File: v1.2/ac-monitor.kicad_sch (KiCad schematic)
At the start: 5 parts, among them U5 MID400

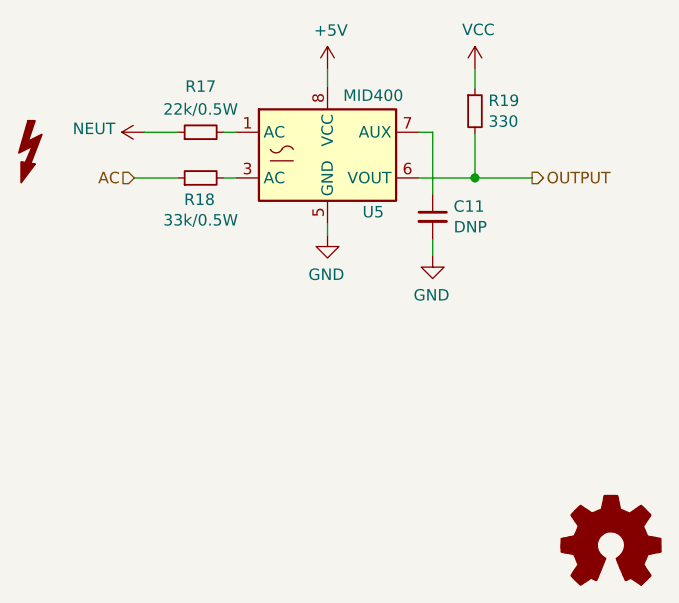
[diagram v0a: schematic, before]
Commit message: place debounce caps for mid400
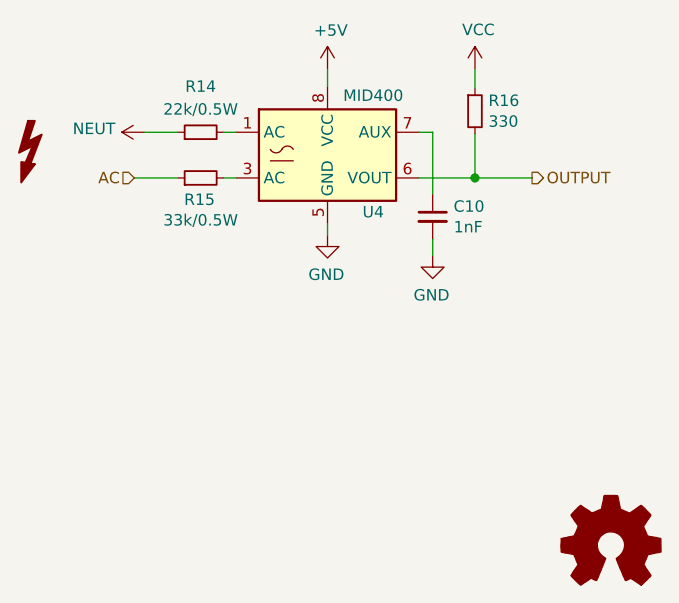
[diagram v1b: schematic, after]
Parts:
- C10: renamed from C11; value DNP -> 1nF
- renumbered R17 to R14, R18 to R15, R19 to R16, U5 to U4
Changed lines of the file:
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@@
   (symbol (lib_id "power:NEUT") (at 83.82 66.04 90)
     (in_bom yes) (on_board yes)
-    (property "Reference" "#PWR040" (id 0) (at 87.63 66.04 0)
+    (property "Reference" "#PWR035" (id 0) (at 87.63 66.04 0)
       (effects (font (size 1.27 1.27)) hide)
     )
@@
   (symbol (lib_id "power:+5V") (at 104.14 59.055 0)
     (in_bom yes) (on_board yes)
-    (property "Reference" "#PWR041" (id 0) (at 104.14 62.865 0)
+    (property "Reference" "#PWR036" (id 0) (at 104.14 62.865 0)
       (effects (font (size 1.27 1.27)) hide)
     )
@@
   (symbol (lib_id "power:VCC") (at 120.523 59.055 0)
     (in_bom yes) (on_board yes)
-    (property "Reference" "#PWR044" (id 0) (at 120.523 62.865 0)
+    (property "Reference" "#PWR039" (id 0) (at 120.523 62.865 0)
       (effects (font (size 1.27 1.27)) hide)
     )
@@
   (symbol (lib_id "power:GND") (at 104.14 77.47 0) (mirror y)
     (in_bom yes) (on_board yes)
-    (property "Reference" "#PWR042" (id 0) (at 104.14 83.82 0)
+    (property "Reference" "#PWR037" (id 0) (at 104.14 83.82 0)
       (effects (font (size 1.27 1.27)) hide)
     )
@@
   (symbol (lib_id "power:GND") (at 115.824 79.756 0) (mirror y)
     (in_bom yes) (on_board yes)
-    (property "Reference" "#PWR043" (id 0) (at 115.824 86.106 0)
+    (property "Reference" "#PWR038" (id 0) (at 115.824 86.106 0)
       (effects (font (size 1.27 1.27)) hide)
     )
@@
   (symbol (lib_id "Device:R_Small") (at 90.043 66.04 90)
     (in_bom yes) (on_board yes)
-    (property "Reference" "R17" (id 0) (at 90.043 60.96 90))
+    (property "Reference" "R14" (id 0) (at 90.043 60.96 90))
     (property "Value" "22k/0.5W" (id 1) (at 90.043 63.5 90))
     (property "Footprint" "Resistor_SMD:R_1206_3216Metric_Pad1.30x1.75mm_HandSolder" (id 2) (at 90.043 66.04 0)
@@
   (symbol (lib_id "Device:R_Small") (at 90.043 71.12 90)
     (in_bom yes) (on_board yes)
-    (property "Reference" "R18" (id 0) (at 89.916 73.533 90))
+    (property "Reference" "R15" (id 0) (at 89.916 73.533 90))
     (property "Value" "33k/0.5W" (id 1) (at 90.043 75.819 90))
     (property "Footprint" "Resistor_SMD:R_1206_3216Metric_Pad1.30x1.75mm_HandSolder" (id 2) (at 90.043 71.12 0)
@@
   (symbol (lib_id "Device:R_Small") (at 120.523 63.7032 0)
     (in_bom yes) (on_board yes)
-    (property "Reference" "R19" (id 0) (at 122.0216 62.5348 0)
+    (property "Reference" "R16" (id 0) (at 122.0216 62.5348 0)
       (effects (font (size 1.27 1.27)) (justify left))
     )
@@
   (symbol (lib_id "Device:C_Small") (at 115.824 75.438 0)
     (in_bom yes) (on_board yes)
-    (property "Reference" "C11" (id 0) (at 118.1482 74.2886 0)
+    (property "Reference" "C10" (id 0) (at 118.1482 74.2886 0)
       (effects (font (size 1.27 1.27)) (justify left))
     )
-    (property "Value" "DNP" (id 1) (at 118.1608 76.581 0)
+    (property "Value" "1nF" (id 1) (at 118.1608 76.581 0)
       (effects (font (size 1.27 1.27)) (justify left))
     )
@@
   (symbol (lib_id "Isolator:MID400") (at 104.14 68.58 0)
     (in_bom yes) (on_board yes)
-    (property "Reference" "U5" (id 0) (at 109.22 74.9108 0))
+    (property "Reference" "U4" (id 0) (at 109.22 74.9108 0))
     (property "Value" "MID400" (id 1) (at 109.22 61.9695 0))
     (property "Footprint" "Package_DIP:SMDIP-8_W7.62mm" (id 2) (at 104.14 68.58 0)

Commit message: More updates
* make pump triac switch NEUT, not LINE
* move ADC a bit
* improve clearance
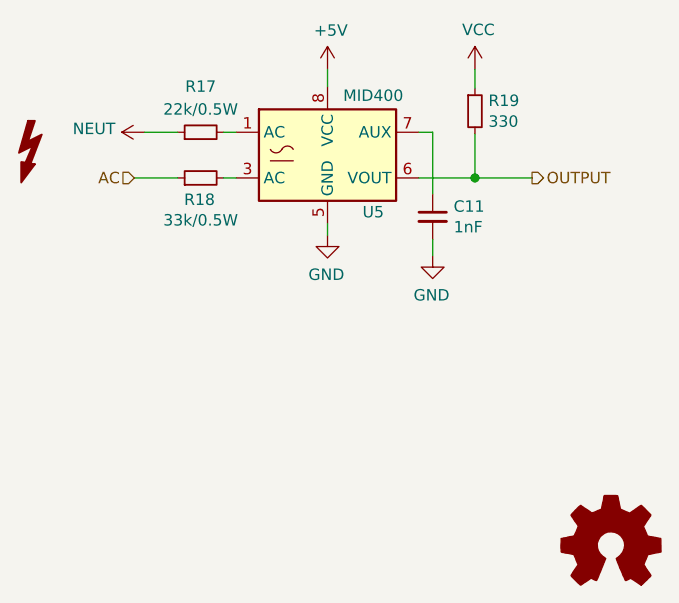
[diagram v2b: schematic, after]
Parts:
- renumbered C10 to C11, R14 to R17, R15 to R18, R16 to R19, U4 to U5
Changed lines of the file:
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@@
 (kicad_sch (version 20201015) (generator eeschema)
-  (page 0 6)
   (paper "A5")
   (title_block
@@
   (symbol (lib_id "power:NEUT") (at 83.82 66.04 90)
     (in_bom yes) (on_board yes)
-    (property "Reference" "#PWR035" (id 0) (at 87.63 66.04 0)
+    (property "Reference" "#PWR040" (id 0) (at 87.63 66.04 0)
       (effects (font (size 1.27 1.27)) hide)
     )
@@
   (symbol (lib_id "power:+5V") (at 104.14 59.055 0)
     (in_bom yes) (on_board yes)
-    (property "Reference" "#PWR036" (id 0) (at 104.14 62.865 0)
+    (property "Reference" "#PWR041" (id 0) (at 104.14 62.865 0)
       (effects (font (size 1.27 1.27)) hide)
     )
@@
   (symbol (lib_id "power:VCC") (at 120.523 59.055 0)
     (in_bom yes) (on_board yes)
-    (property "Reference" "#PWR039" (id 0) (at 120.523 62.865 0)
+    (property "Reference" "#PWR044" (id 0) (at 120.523 62.865 0)
       (effects (font (size 1.27 1.27)) hide)
     )
@@
   (symbol (lib_id "power:GND") (at 104.14 77.47 0) (mirror y)
     (in_bom yes) (on_board yes)
-    (property "Reference" "#PWR037" (id 0) (at 104.14 83.82 0)
+    (property "Reference" "#PWR042" (id 0) (at 104.14 83.82 0)
       (effects (font (size 1.27 1.27)) hide)
     )
@@
   (symbol (lib_id "power:GND") (at 115.824 79.756 0) (mirror y)
     (in_bom yes) (on_board yes)
-    (property "Reference" "#PWR038" (id 0) (at 115.824 86.106 0)
+    (property "Reference" "#PWR043" (id 0) (at 115.824 86.106 0)
       (effects (font (size 1.27 1.27)) hide)
     )
@@
   (symbol (lib_id "Device:R_Small") (at 90.043 66.04 90)
     (in_bom yes) (on_board yes)
-    (property "Reference" "R14" (id 0) (at 90.043 60.96 90))
+    (property "Reference" "R17" (id 0) (at 90.043 60.96 90))
     (property "Value" "22k/0.5W" (id 1) (at 90.043 63.5 90))
     (property "Footprint" "Resistor_SMD:R_1206_3216Metric_Pad1.30x1.75mm_HandSolder" (id 2) (at 90.043 66.04 0)
@@
   (symbol (lib_id "Device:R_Small") (at 90.043 71.12 90)
     (in_bom yes) (on_board yes)
-    (property "Reference" "R15" (id 0) (at 89.916 73.533 90))
+    (property "Reference" "R18" (id 0) (at 89.916 73.533 90))
     (property "Value" "33k/0.5W" (id 1) (at 90.043 75.819 90))
     (property "Footprint" "Resistor_SMD:R_1206_3216Metric_Pad1.30x1.75mm_HandSolder" (id 2) (at 90.043 71.12 0)
@@
   (symbol (lib_id "Device:R_Small") (at 120.523 63.7032 0)
     (in_bom yes) (on_board yes)
-    (property "Reference" "R16" (id 0) (at 122.0216 62.5348 0)
+    (property "Reference" "R19" (id 0) (at 122.0216 62.5348 0)
       (effects (font (size 1.27 1.27)) (justify left))
     )
@@
   (symbol (lib_id "Device:C_Small") (at 115.824 75.438 0)
     (in_bom yes) (on_board yes)
-    (property "Reference" "C10" (id 0) (at 118.1482 74.2886 0)
+    (property "Reference" "C11" (id 0) (at 118.1482 74.2886 0)
       (effects (font (size 1.27 1.27)) (justify left))
     )
@@
   (symbol (lib_id "Isolator:MID400") (at 104.14 68.58 0)
     (in_bom yes) (on_board yes)
-    (property "Reference" "U4" (id 0) (at 109.22 74.9108 0))
+    (property "Reference" "U5" (id 0) (at 109.22 74.9108 0))
     (property "Value" "MID400" (id 1) (at 109.22 61.9695 0))
     (property "Footprint" "Package_DIP:SMDIP-8_W7.62mm" (id 2) (at 104.14 68.58 0)
